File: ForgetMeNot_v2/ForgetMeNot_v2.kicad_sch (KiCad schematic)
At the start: 45 parts, among them J1 Conn_01x04, SW1 SW_Push, U1 RP2040, U2 W25Q128JVS, U3 NCP1117, U4 LIS2HH12, U5 MCP1640x-xMC, Y1 Crystal_ABM8

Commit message: Updated inductor
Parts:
- L1: footprint Inductor_SMD:L_0402_1005Metric -> Inductor_SMD:L_1008_2520Metric
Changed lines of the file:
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@@
 			)
 		)
-		(property "Footprint" "Inductor_SMD:L_0402_1005Metric"
+		(property "Footprint" "Inductor_SMD:L_1008_2520Metric"
 			(at 158.75 62.23 0)
 			(effects

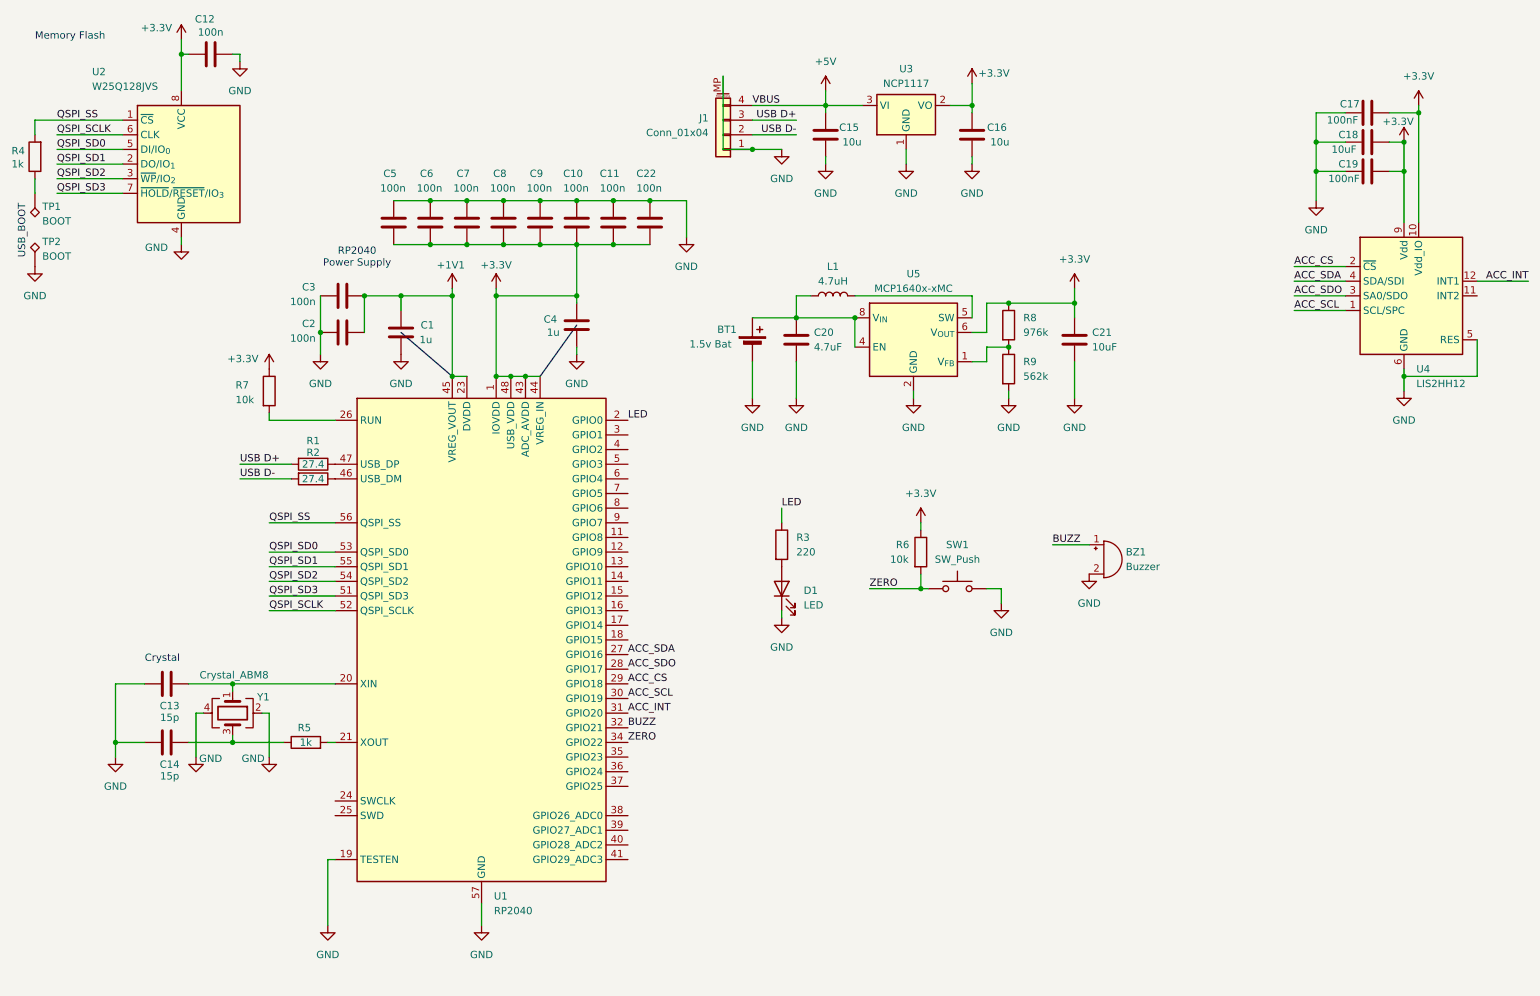
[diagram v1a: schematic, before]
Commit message: removed ncp1117 so that the board is always powered by the battery and not the case of sometimes powered by the usb. (reduces complexity)
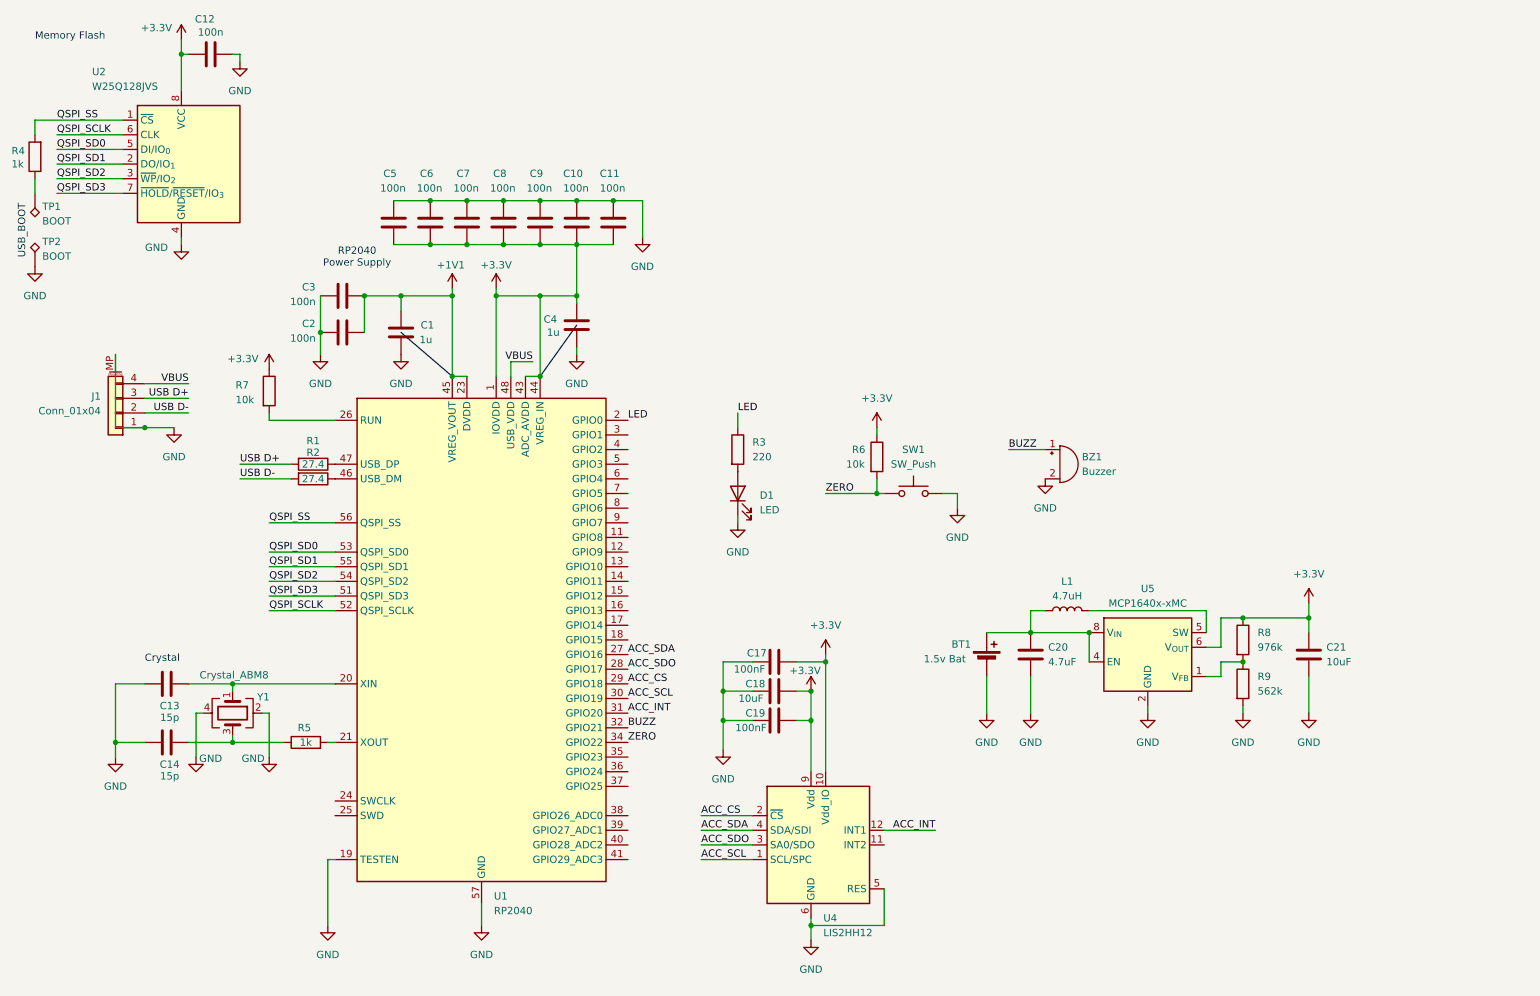
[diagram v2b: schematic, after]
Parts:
- removed C11: 100n, Capacitor_SMD:C_0402_1005Metric, symbol Device:C
- removed C15, C16: 10u, Capacitor_SMD:C_0402_1005Metric, symbol Device:C
- removed U3: NCP1117, Package_TO_SOT_SMD:SOT-223-3_TabPin2, symbol Regulator_Linear:NCP1117-3.3_SOT223
- renumbered C22 to C11
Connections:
- net +3.3V: no longer U1.48 (USB_VDD)
- net +5V renamed VBUS
- net VBUS: now also U1.48 (USB_VDD)
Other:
- moved on the sheet: BT1, BZ1, C11, C17, C18, C19, C20, C21, D1, J1, L1, R3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

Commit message: test points
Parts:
- added TP3: 3v3, TestPoint:TestPoint_THTPad_D1.0mm_Drill0.5mm, symbol Connector:TestPoint
- added TP4: SDA, TestPoint:TestPoint_THTPad_D1.0mm_Drill0.5mm, symbol Connector:TestPoint
- added TP5: SCL, TestPoint:TestPoint_THTPad_D1.0mm_Drill0.5mm, symbol Connector:TestPoint
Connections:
- net +3.3V: now also TP3.1
- net ACC_SCL: now also TP5.1
- net ACC_SDA: now also TP4.1

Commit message: added test points
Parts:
- TP4, TP5: footprint TestPoint:TestPoint_THTPad_D1.0mm_Drill0.5mm -> TestPoint:TestPoint_Pad_D1.0mm
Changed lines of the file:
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@@
 			)
 		)
-		(property "Footprint" "TestPoint:TestPoint_THTPad_D1.0mm_Drill0.5mm"
+		(property "Footprint" "TestPoint:TestPoint_Pad_D1.0mm"
 			(at 162.56 46.99 0)
 			(effects
@@
 			)
 		)
-		(property "Footprint" "TestPoint:TestPoint_THTPad_D1.0mm_Drill0.5mm"
+		(property "Footprint" "TestPoint:TestPoint_Pad_D1.0mm"
 			(at 173.99 46.99 0)
 			(effects

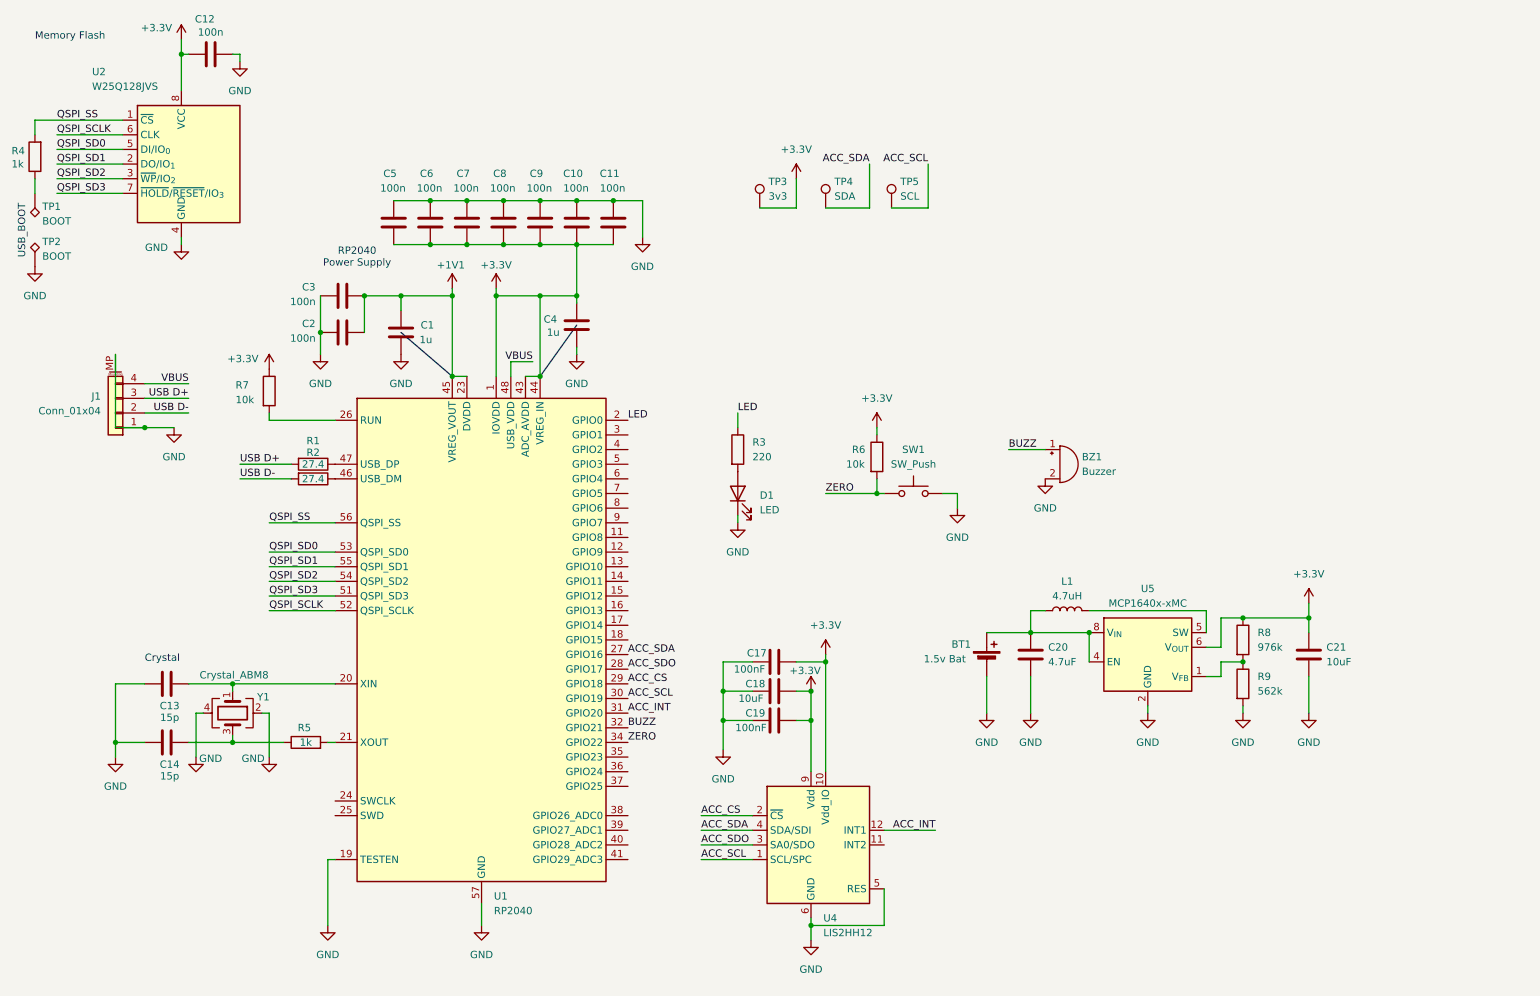
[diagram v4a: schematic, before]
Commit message: updated MCU from RP2040 to ATmega328p
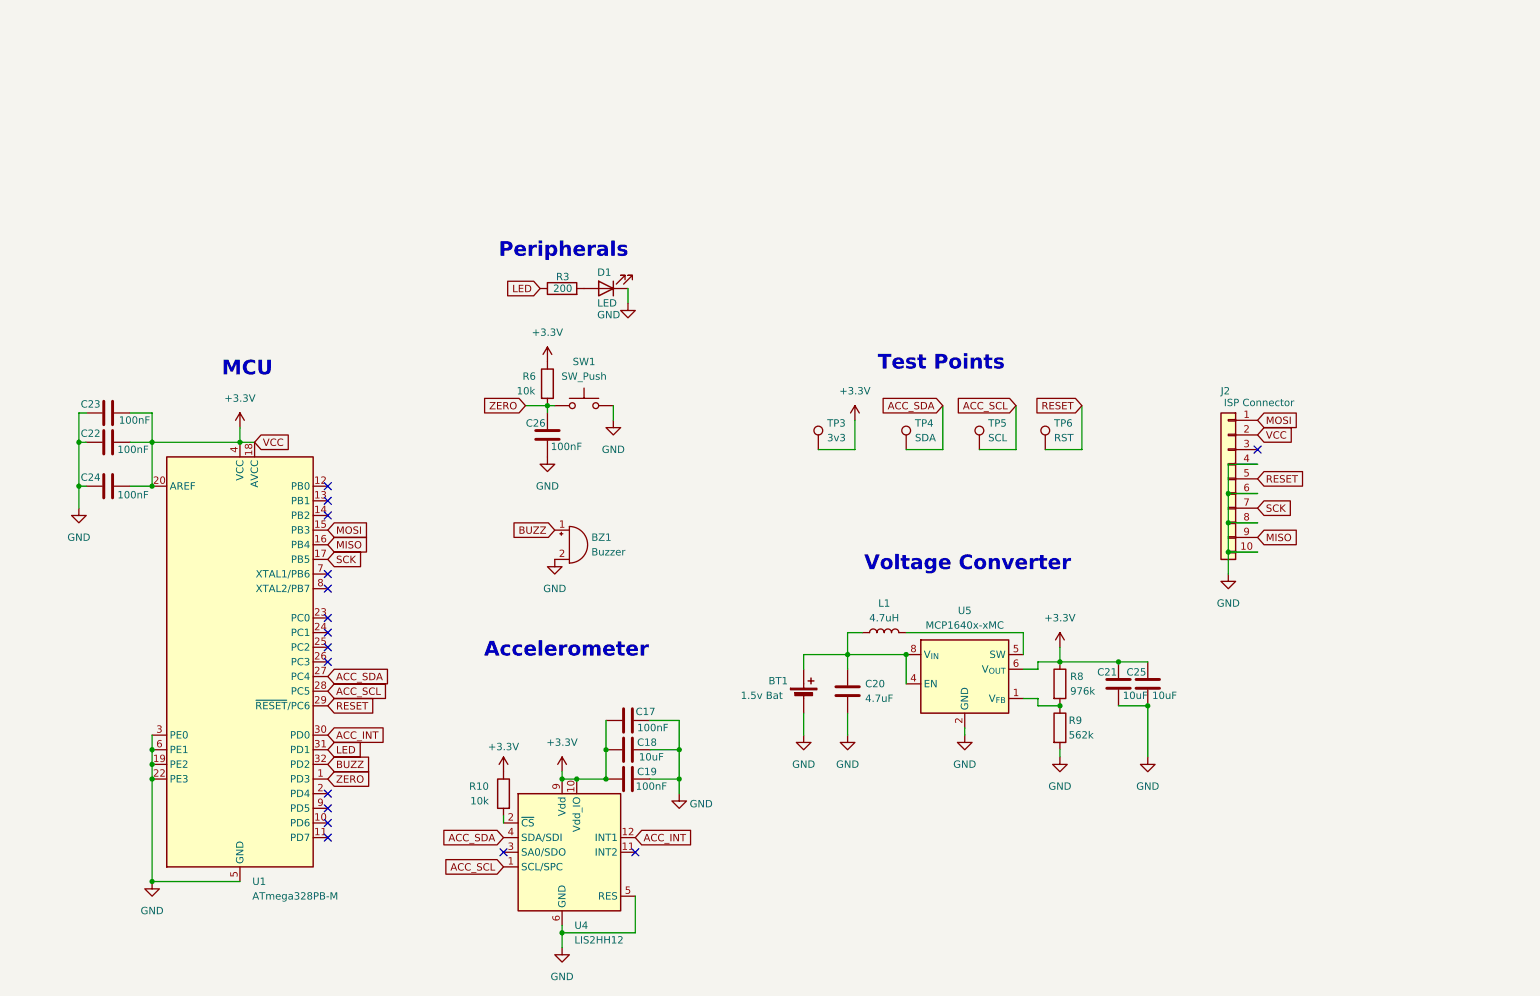
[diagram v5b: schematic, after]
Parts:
- removed C1, C4: 1u, Capacitor_SMD:C_0402_1005Metric, symbol Device:C
- removed C10, C11, C12, C2, C3, C5, C6, C7, C8, C9: 100n, Capacitor_SMD:C_0402_1005Metric, symbol Device:C
- removed C13, C14: 15p, Capacitor_SMD:C_0402_1005Metric, symbol Device:C
- removed J1: Conn_01x04, Connector_Molex:Molex_CLIK-Mate_502585-0470_1x04-1MP_P1.50mm_Horizontal, symbol Connector_Generic_MountingPin:Conn_01x04_MountingPin
- removed R1, R2: 27.4, Resistor_SMD:R_0402_1005Metric, symbol Device:R
- removed R4, R5: 1k, Resistor_SMD:R_0402_1005Metric, symbol Device:R
- removed R7: 10k, Resistor_SMD:R_0402_1005Metric, symbol Device:R
- removed TP1: BOOT, TestPoint:TestPoint_THTPad_1.0x1.0mm_Drill0.5mm, symbol Connector:TestPoint_Alt
- removed TP2: BOOT, TestPoint:TestPoint_THTPad_D1.0mm_Drill0.5mm, symbol Connector:TestPoint_Alt
- removed U1: RP2040, Package_DFN_QFN:QFN-56-1EP_7x7mm_P0.4mm_EP3.2x3.2mm, symbol MCU_RaspberryPi:RP2040
- removed U2: W25Q128JVS, Package_SO:SOIC-8_5.3x5.3mm_P1.27mm, symbol Memory_Flash:W25Q128JVS
- removed Y1: Crystal_ABM8, Crystal:ABM8, symbol Device:Crystal_GND24
- added C22, C23, C24, C26: 100nF, Capacitor_SMD:C_0402_1005Metric, symbol Device:C
- added C25: 10uF, Capacitor_SMD:C_0402_1005Metric, symbol Device:C
- added J2: ISP Connector, Connector_PCBEdge:Samtec_MECF-05-0_-NP-L-DV_2x05_P1.27mm_Edge, symbol Connector_Generic:Conn_01x10
- added R10: 10k, Resistor_SMD:R_0402_1005Metric, symbol Device:R
- added TP6: RST, TestPoint:TestPoint_THTPad_D1.0mm_Drill0.5mm, symbol Connector:TestPoint
- added U1: ATmega328PB-M, Package_DFN_QFN:QFN-32-1EP_5x5mm_P0.5mm_EP3.1x3.1mm, symbol MCU_Microchip_ATmega:ATmega328PB-M
- R3: value 220 -> 200
- SW1: footprint Button_Switch_SMD:SW_SPST_PTS647_Sx38 -> Button_Switch_SMD:SW_SPST_PTS810
- TP4, TP5: footprint TestPoint:TestPoint_Pad_D1.0mm -> TestPoint:TestPoint_THTPad_D1.0mm_Drill0.5mm
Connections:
- net +3.3V: now also C21.2, C22.2, C23.2, C24.2, C25.2, J2.2 (Pin_2), R10.1, U1.18 (AVCC), U1.20 (AREF), U1.4 (VCC); no longer C21.1
- net ACC_INT: now also U1.30 (PD0)
- net ACC_SCL: now also U1.28 (PC5)
- net ACC_SDA: now also U1.27 (PC4)
- net BUZZ: now also U1.32 (PD2)
- net GND: now also C21.1, C22.1, C23.1, C24.1, C25.1, C26.2, J2.10 (Pin_10), J2.4 (Pin_4), J2.6 (Pin_6), J2.8 (Pin_8), U1.19 (PE2), U1.21 (GND), U1.22 (PE3), U1.3 (PE0), U1.33 (GND), U1.5 (GND), U1.6 (PE1); no longer C21.2
- net LED: now also U1.31 (PD1)
- net ZERO: now also C26.1, U1.1 (PD3)
- net ACC_CS: no longer names the net of U4.2 (~{CS})
- net ACC_CS: now also R10.2
- net ACC_SDO: no longer names the net of U4.3 (SA0/SDO)
- new net MISO: J2.9 (Pin_9), U1.16 (PB4)
- new net MOSI: J2.1 (Pin_1), U1.15 (PB3)
- new net RESET: J2.5 (Pin_5), TP6.1, U1.29 (~{RESET}/PC6)
- new net SCK: J2.7 (Pin_7), U1.17 (PB5)
- no-connect marks 0 -> 16
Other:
- note added: "Accelerometer"
- note added: "MCU"
- note added: "Peripherals"
- note added: "Test Points"
- note added: "Voltage Converter"
- note removed: "Crystal"
- note removed: "Memory Flash"
- note removed: "RP2040 Power Supply"
- note removed: "USB_BOOT"
- moved on the sheet: BT1, BZ1, C17, C18, C19, C20, C21, D1, L1, R3, R6, R8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

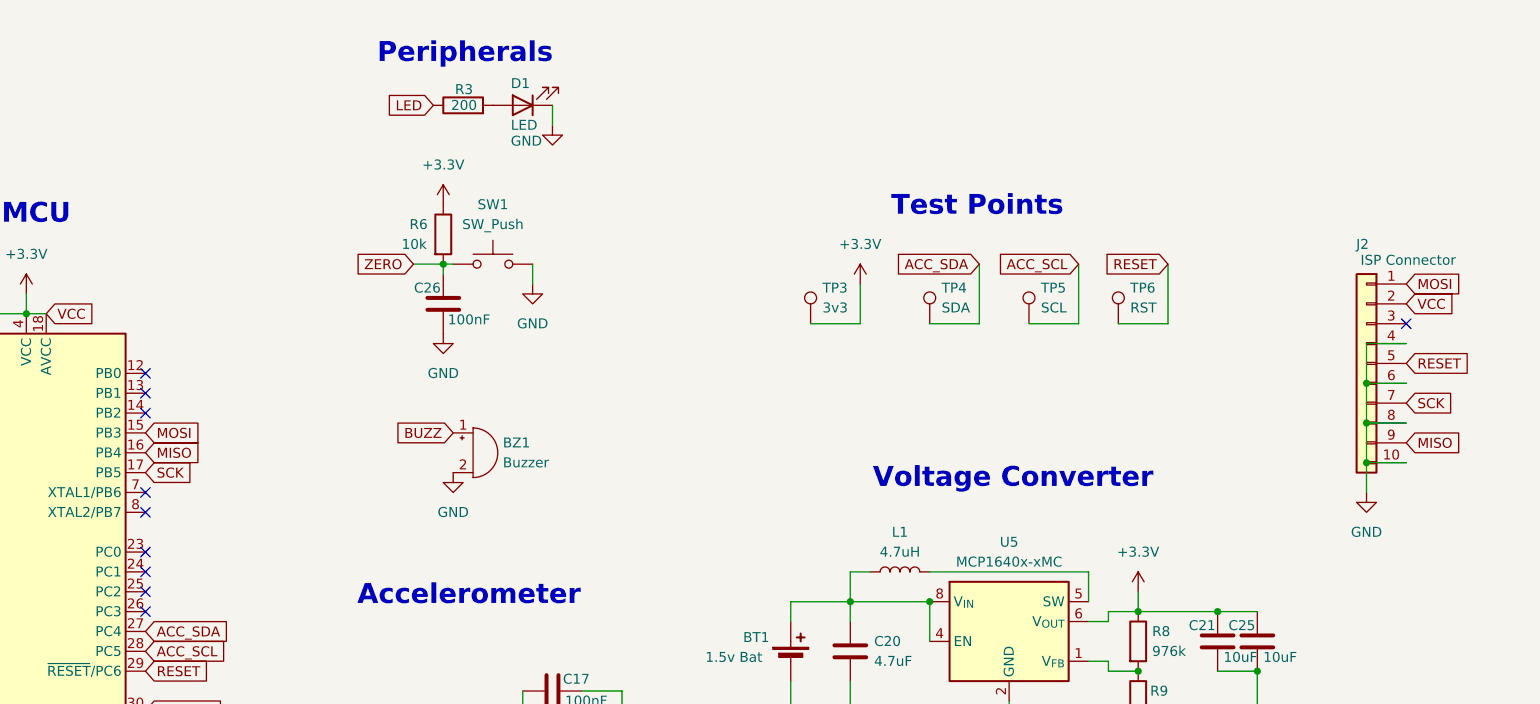
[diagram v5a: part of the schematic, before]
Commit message: changed connector
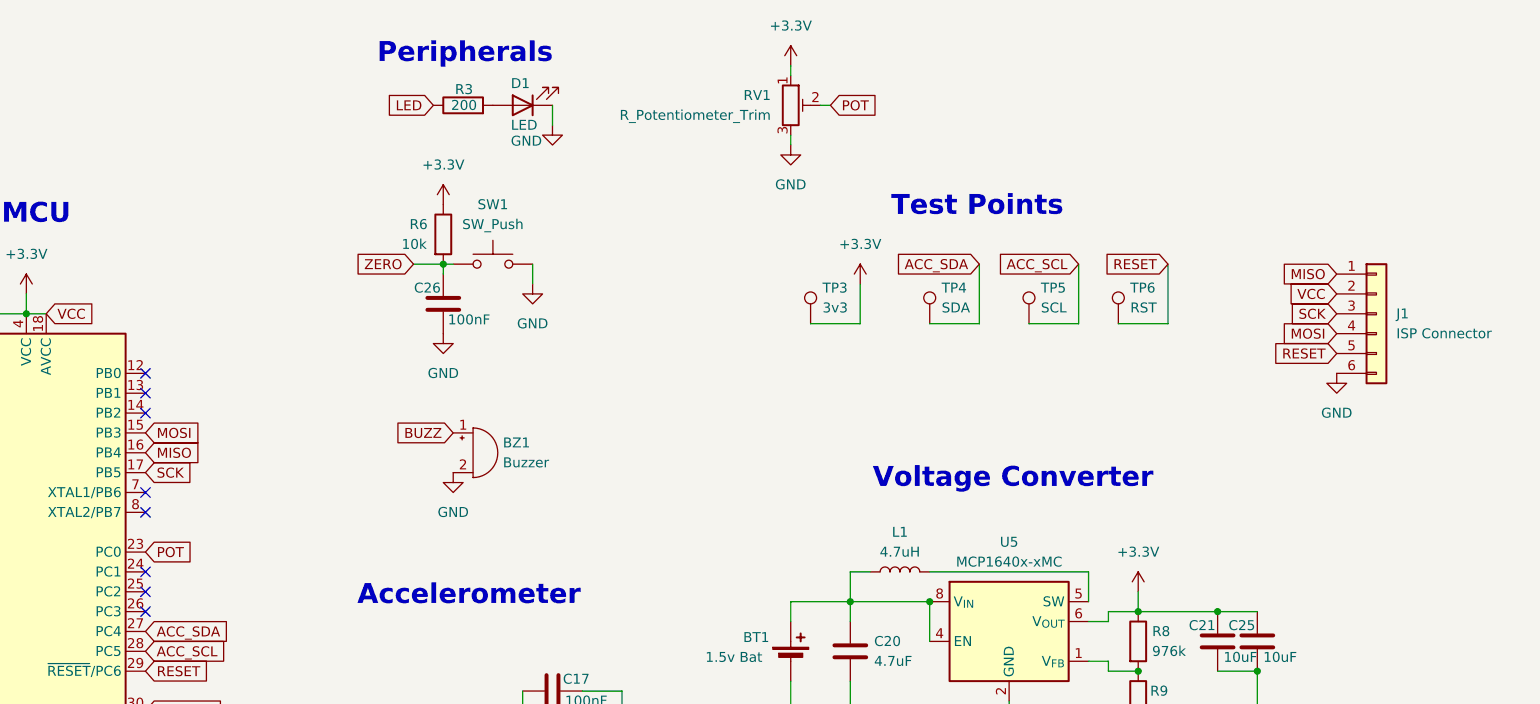
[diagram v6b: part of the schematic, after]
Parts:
- removed J2: ISP Connector, Connector_PCBEdge:Samtec_MECF-05-0_-NP-L-DV_2x05_P1.27mm_Edge, symbol Connector_Generic:Conn_01x10
- added J1: ISP Connector, Connector_Molex:Molex_Micro-Latch_53254-0670_1x06_P2.00mm_Horizontal, symbol Connector_Generic:Conn_01x06
- added RV1: R_Potentiometer_Trim, Potentiometer_SMD:Potentiometer_Bourns_TC33X_Vertical, symbol Device:R_Potentiometer_Trim
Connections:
- net +3.3V: now also J1.2 (Pin_2), RV1.1
- net GND: now also J1.6 (Pin_6), RV1.3
- net MISO: now also J1.1 (Pin_1)
- net MOSI: now also J1.4 (Pin_4)
- net RESET: now also J1.5 (Pin_5)
- net SCK: now also J1.3 (Pin_3)
- net POT: now reaches U1.23 (PC0)
- net POT: now also RV1.2
- no-connect marks 16 -> 14
